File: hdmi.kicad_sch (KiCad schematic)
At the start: 37 parts, among them J3 HDMI_A, Q1 2N7002, Q2 2SK3018, Q3 2SK3018, Q4 2SK3018, U1 D3V3XA4B10LP, U2 D3V3XA4B10LP

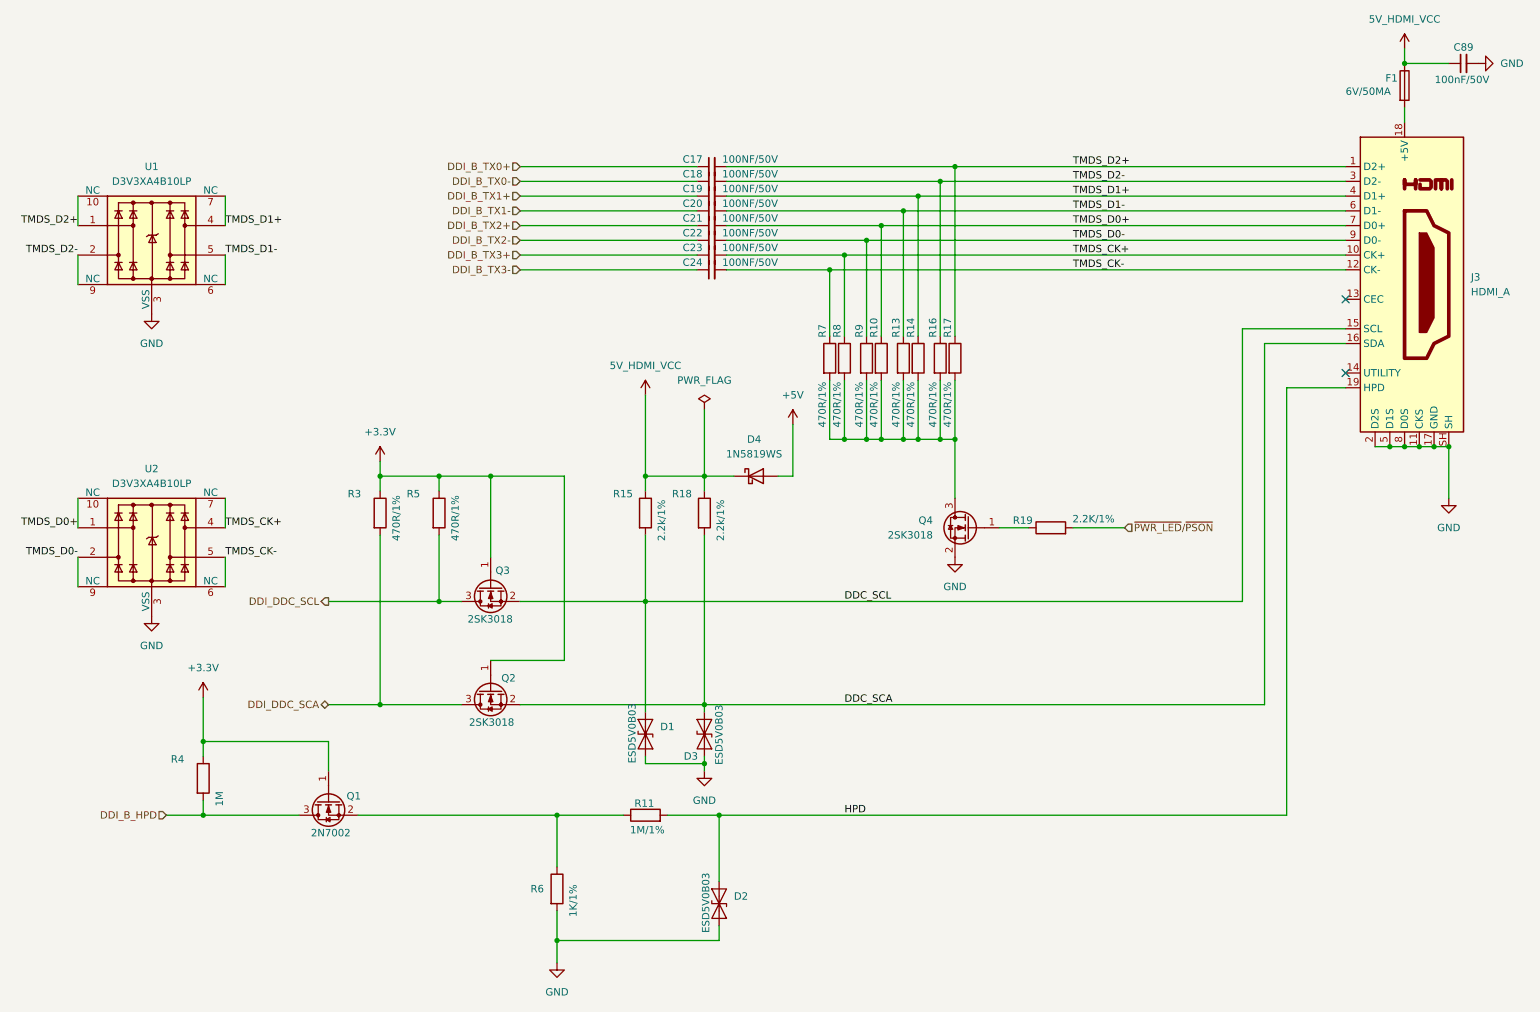
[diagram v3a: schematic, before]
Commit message: Updated all the footprints into the pcb editor but all the designator numbers have changed... I have tp go back and fix each one
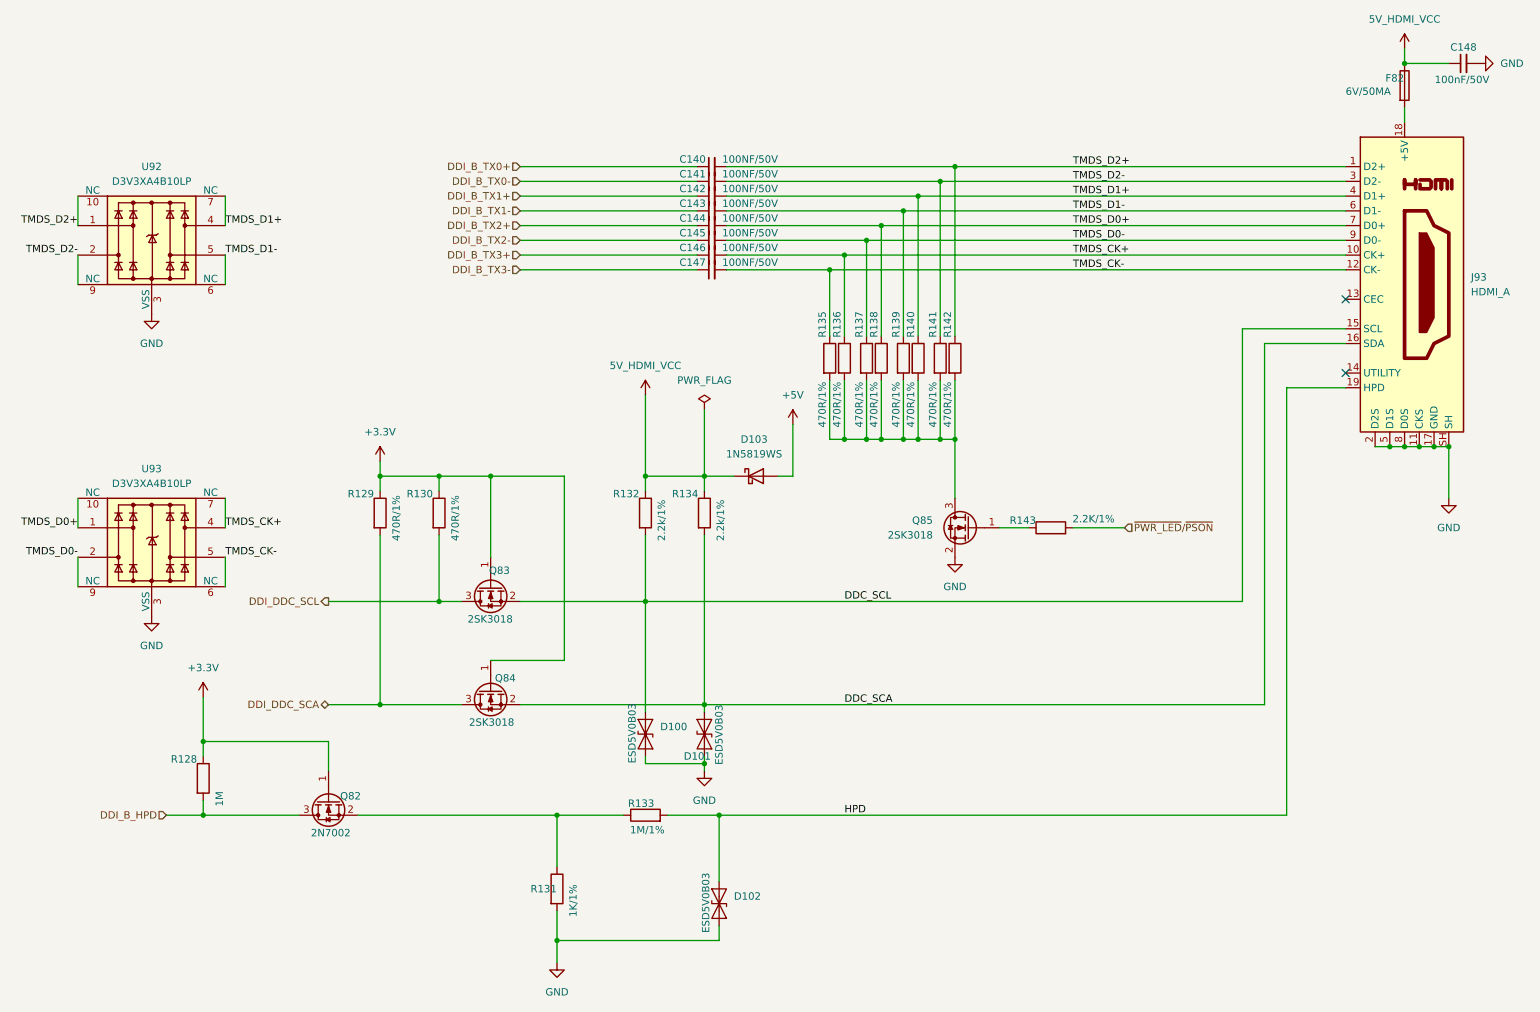
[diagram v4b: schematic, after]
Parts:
- C148: renamed from C89; footprint (none) -> A_HDJ_Library:C_0402_1005Metric
- renumbered C17 to C140, C18 to C141, C19 to C142, C20 to C143, C21 to C144, C22 to C145, C23 to C146, C24 to C147, D1 to D100, D3 to D101, D2 to D102, D4 to D103, F1 to F82, J3 to J93, Q1 to Q82, Q3 to Q83, Q2 to Q84, Q4 to Q85, R4 to R128, R3 to R129, R5 to R130, R6 to R131, R15 to R132, R11 to R133, R18 to R134, R7 to R135, R8 to R136, R9 to R137, R10 to R138, R13 to R139, R14 to R140, R16 to R141, R17 to R142, R19 to R143, U1 to U92, U2 to U93

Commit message: Designators in HDMI restored
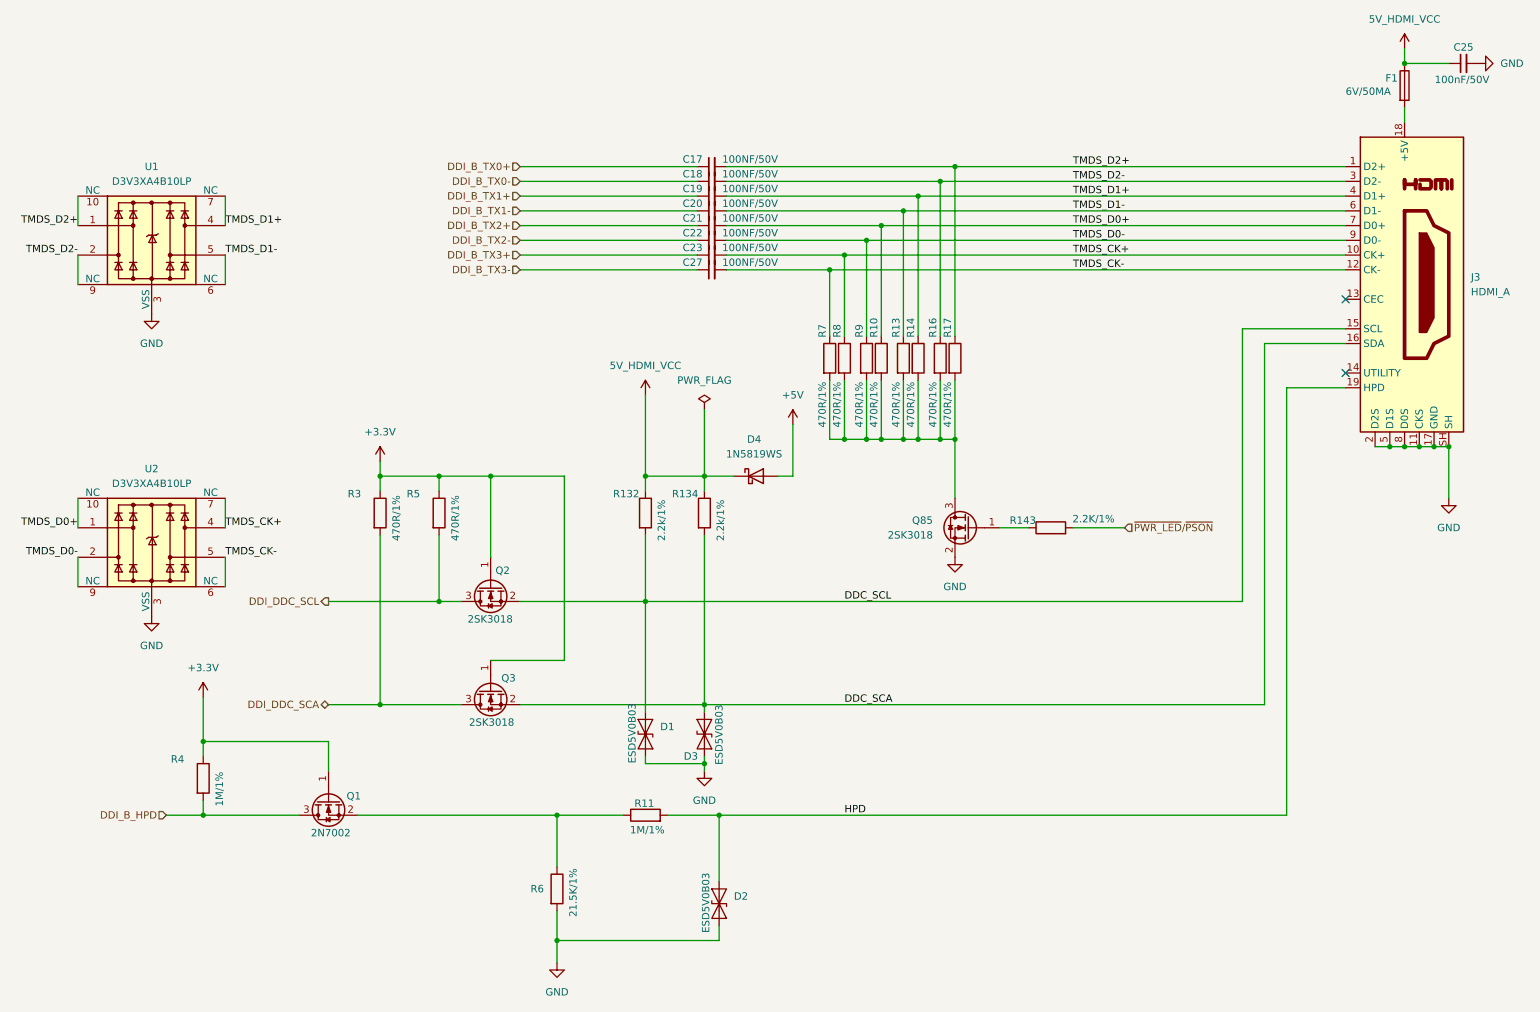
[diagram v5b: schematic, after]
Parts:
- R4: renamed from R128; value 1M -> 1M/1%
- R6: renamed from R131; value 1K/1% -> 21.5K/1%
- renumbered C140 to C17, C141 to C18, C142 to C19, C143 to C20, C144 to C21, C145 to C22, C146 to C23, C148 to C25, C147 to C27, D100 to D1, D102 to D2, D101 to D3, D103 to D4, F82 to F1, J93 to J3, Q82 to Q1, Q83 to Q2, Q84 to Q3, R138 to R10, R133 to R11, R139 to R13, R140 to R14, R141 to R16, R142 to R17, R129 to R3, R130 to R5, R135 to R7, R136 to R8, R137 to R9, U92 to U1, U93 to U2
